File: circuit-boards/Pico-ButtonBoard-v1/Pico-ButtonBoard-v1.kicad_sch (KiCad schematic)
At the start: 27 parts, among them J19 CAN, J20 CAN, J21 BATT, J22 DC_IN, U4 4.0 MHz, U5 MCP2518FDT-H/SL, U8 MCP2558FD

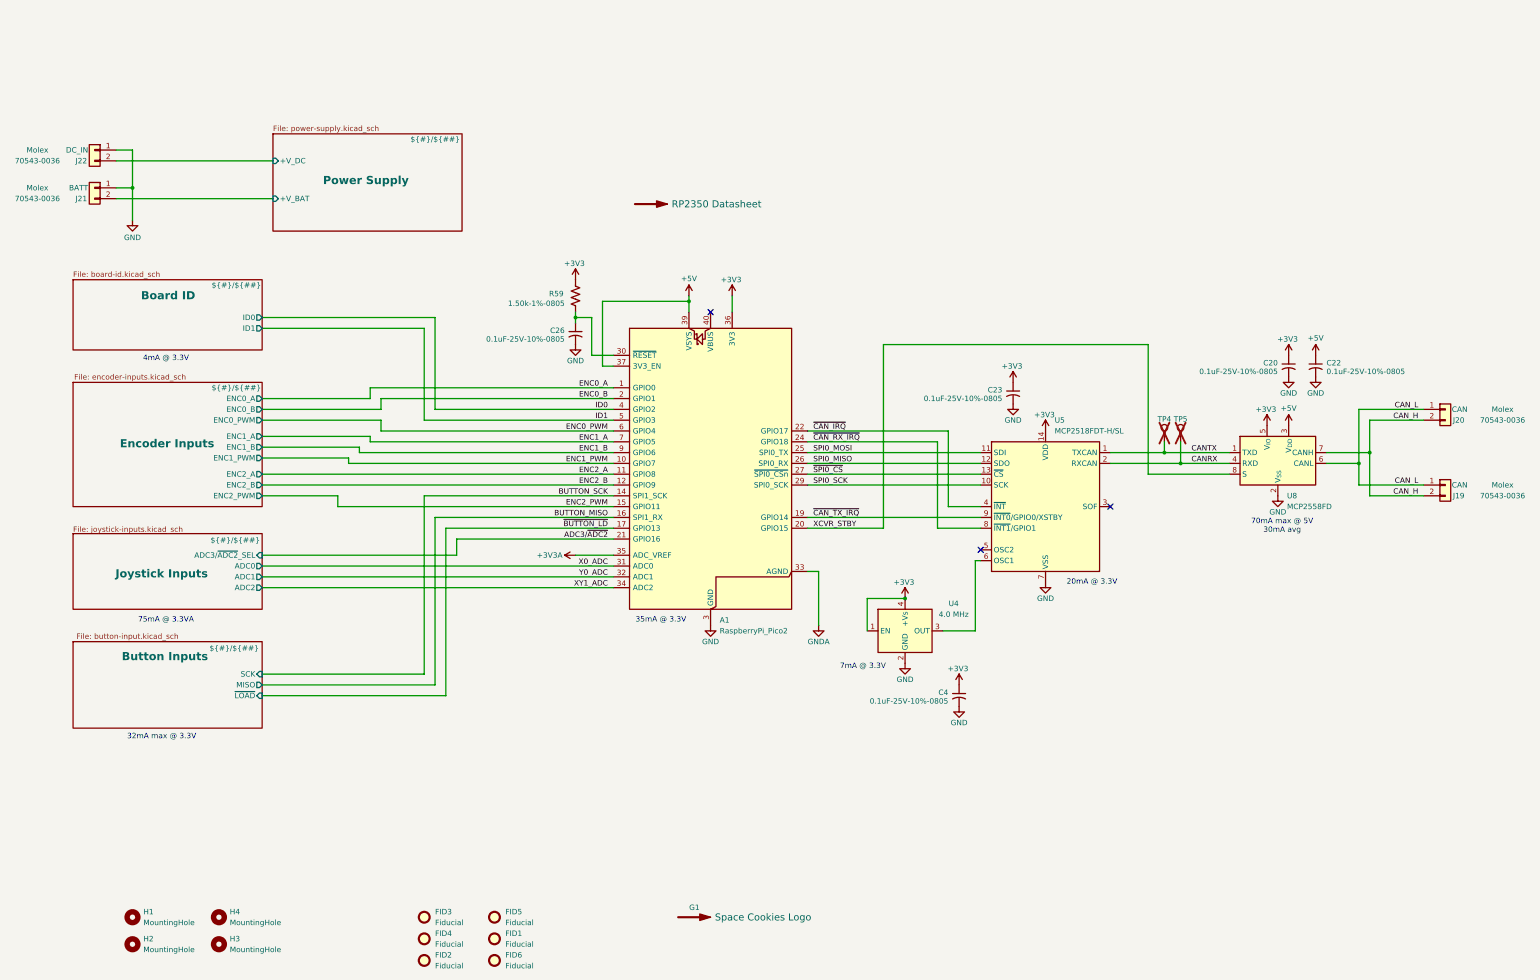
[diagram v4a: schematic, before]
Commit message: Changed button input circuit to use mux. Changed ADC3 to an external SPI ADC
Signed-off-by: Scott Berman <sgberman1@gmail.com>
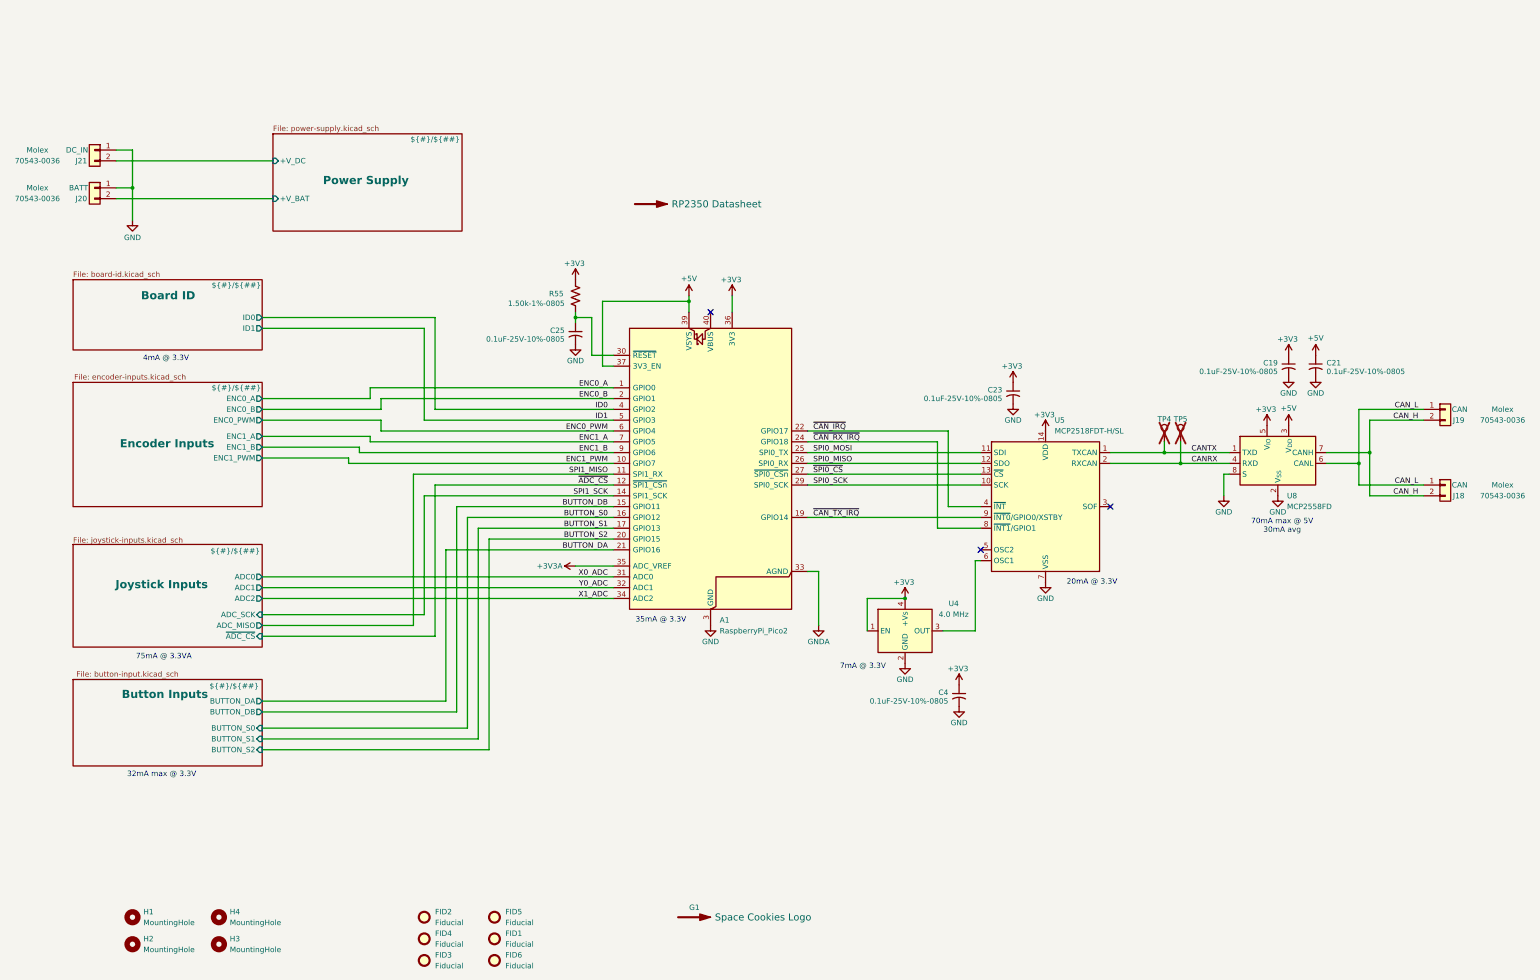
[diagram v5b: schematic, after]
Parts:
- renumbered C20 to C19, C22 to C21, C26 to C25, FID3 to FID2, FID2 to FID3, J19 to J18, J20 to J19, J21 to J20, J22 to J21, R59 to R55
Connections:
- net GND: now also U8.8 (S)
- net ADC3/~{ADC2} renamed BUTTON_DA
- net BUTTON_MISO renamed BUTTON_S0
- net BUTTON_SCK renamed SPI1_SCK
- net ENC2_A renamed SPI1_MISO
- net ENC2_B renamed ~{ADC_CS}
- net ENC2_PWM renamed BUTTON_DB
- net XCVR_STBY renamed BUTTON_S2
- net BUTTON_S2: no longer U8.8 (S)
- net XY1_ADC renamed X1_ADC
- net ~{BUTTON_LD} renamed BUTTON_S1
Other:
- sheet Button Inputs ports: added BUTTON_DA, BUTTON_DB, BUTTON_S0, BUTTON_S1, BUTTON_S2; removed MISO, SCK, ~{LOAD}
- sheet Encoder Inputs ports: added none; removed ENC2_A, ENC2_B, ENC2_PWM
- sheet Joystick Inputs ports: added ADC_MISO, ADC_SCK, ~{ADC_CS}; removed ADC3/~{ADC2}_SEL

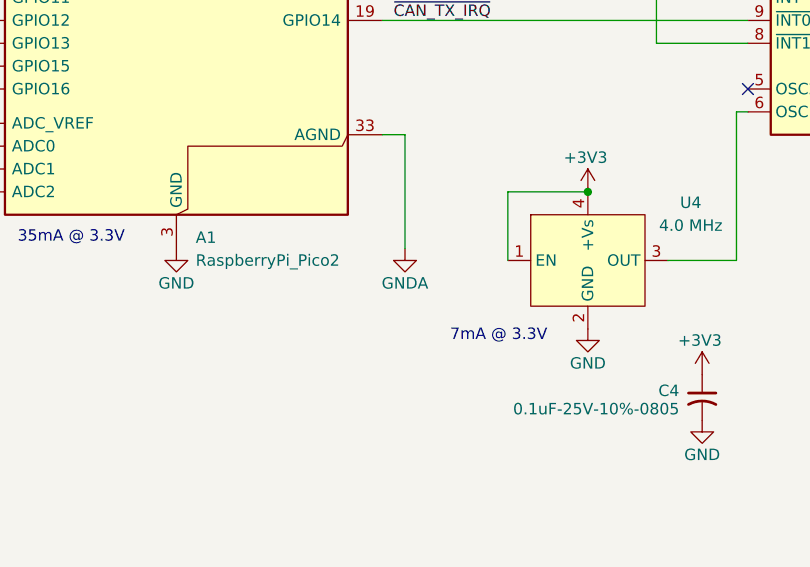
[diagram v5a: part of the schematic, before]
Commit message: Minor schematic fix
Signed-off-by: Scott Berman <sgberman1@gmail.com>
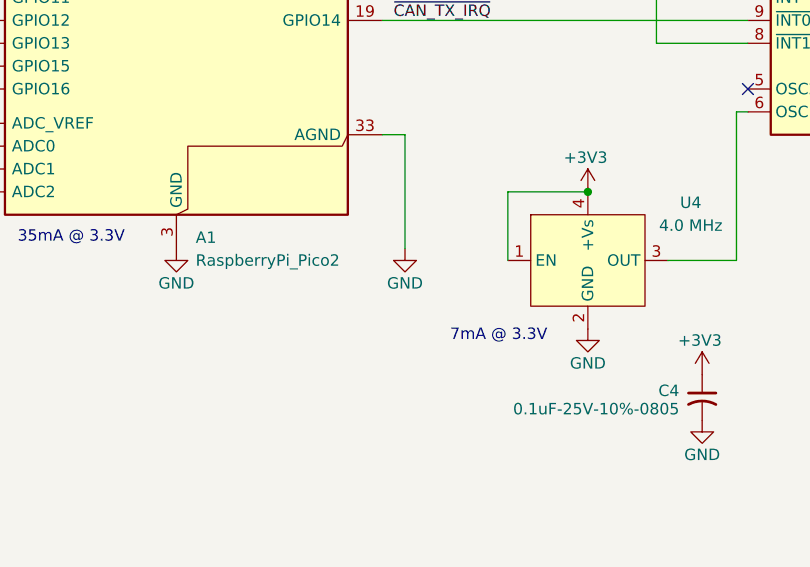
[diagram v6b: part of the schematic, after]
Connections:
- net GNDA is gone; now on net GND: A1.33 (AGND)
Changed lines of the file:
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@@
 	)
 	(symbol
-		(lib_id "power:GND")
-		(at 229.87 172.72 0)
-		(unit 1)
-		(exclude_from_sim no)
-		(in_bom yes)
-		(on_board yes)
-		(dnp no)
-		(property "Reference" "#PWR0108"
-			(at 229.87 179.07 0)
-			(effects
-				(font
-					(size 1.27 1.27)
-				)
-				(hide yes)
-			)
-		)
-		(property "Value" "GNDA"
-			(at 229.87 176.53 0)
-			(effects
-				(font
-					(size 1.27 1.27)
-				)
-			)
-		)
-		(property "Footprint" ""
-			(at 229.87 172.72 0)
-			(effects
-				(font
-					(size 1.27 1.27)
-				)
-				(hide yes)
-			)
-		)
-		(property "Datasheet" ""
-			(at 229.87 172.72 0)
-			(effects
-				(font
-					(size 1.27 1.27)
-				)
-				(hide yes)
-			)
-		)
-		(property "Description" ""
-			(at 229.87 172.72 0)
-			(effects
-				(font
-					(size 1.27 1.27)
-				)
-				(hide yes)
-			)
-		)
-		(pin "1"
-		)
-		(instances
-			(project "Pico-ButtonBoard-v1"
-				(path "/644201a9-3a2f-4df3-9c93-2ae55394df4b"
-					(reference "#PWR0108")
-					(unit 1)
-				)
-			)
-		)
-	)
-	(symbol
 		(lib_id "Mechanical:Fiducial")
 		(at 153.67 246.38 0)
@@
 					(unit 1)
 				)
+			)
+		)
+	)
+	(symbol
+		(lib_id "power:GND")
+		(at 229.87 172.72 0)
+		(unit 1)
+		(exclude_from_sim no)
+		(in_bom yes)
+		(on_board yes)
+		(dnp no)
+		(property "Reference" "#PWR0108"
+			(at 229.87 179.07 0)
+			(effects
+				(font
+					(size 1.27 1.27)
+				)
+				(hide yes)
+			)
+		)
+		(property "Value" "GND"
+			(at 229.87 176.53 0)
+			(effects
+				(font
+					(size 1.27 1.27)
+				)
+			)
+		)
+		(property "Footprint" ""
+			(at 229.87 172.72 0)
+			(effects
+				(font
+					(size 1.27 1.27)
+				)
+				(hide yes)
+			)
+		)
+		(property "Datasheet" ""
+			(at 229.87 172.72 0)
+			(effects
+				(font
+					(size 1.27 1.27)
+				)
+				(hide yes)
+			)
+		)
+		(property "Description" ""
+			(at 229.87 172.72 0)
+			(effects
+				(font
+					(size 1.27 1.27)
+				)
+				(hide yes)
+			)
+		)
+		(pin "1"
+		)
+		(instances
+			(project "Pico-ButtonBoard-v1"
+				(path "/644201a9-3a2f-4df3-9c93-2ae55394df4b"
+					(reference "#PWR0108")
+					(unit 1)
+				)

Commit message: Add power over CAN to supply joystick from button interfaces.
Signed-off-by: Scott Berman <sgberman1@gmail.com>
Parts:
- removed J18: CAN, Pico-ButtonBoard:Molex-70543-0001, symbol Connector_Generic:Conn_01x02
- added J18: CAN, Pico-ButtonBoard:Molex-70543-0003, symbol Connector_Generic:Conn_01x04
- renumbered C19 to C17, C21 to C19, TP4 to TP5, TP5 to TP6
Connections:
- net CAN_H: now also J18.4 (Pin_4)
- net CAN_L: now also J18.3 (Pin_3)
- net GND: now also J18.1 (Pin_1)
- new net V_PS: J18.2 (Pin_2)
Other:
- sheet Power Supply ports: added V_PS; removed none
- moved on the sheet: J19
